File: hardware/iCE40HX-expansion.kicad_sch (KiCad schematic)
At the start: 3 parts, among them J1 EXT3, J2 EXT1, J4 VGA_Conn

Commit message: porgress with schematic
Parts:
- removed J4: VGA_Conn, symbol Connector:DE15_Plug_HighDensity_MountingHoles
- added C1, C10, C12, C14, C4, C5, C8: 0.1uf, Capacitor_SMD:C_0603_1608Metric, symbol Device:C_Small
- added C11, C13, C15, C6, C9: 10nf, Capacitor_SMD:C_0603_1608Metric, symbol Device:C_Small
- added C2, C3: 47pf, Capacitor_SMD:C_0603_1608Metric, symbol Device:C_Small
- added C7: 82nf, Capacitor_SMD:C_0603_1608Metric, symbol Device:C_Small
- added J3, J5: AudioJack3_Ground, Connector_Audio:Jack_3.5mm_KoreanHropartsElec_PJ-320D-4A_Horizontal, symbol Connector_Audio:AudioJack3_Ground
- added J4: Conn_01x34, C2797218:FPC-SMD_KH-FG0.5-H2.0-34PIN, symbol Connector_Generic:Conn_01x34
- added J6: Conn_01x04, Connector_PinHeader_2.54mm:PinHeader_1x04_P2.54mm_Vertical, symbol Connector_Generic:Conn_01x04
- added J7: Conn_01x06, Connector_PinHeader_2.54mm:PinHeader_1x06_P2.54mm_Vertical, symbol Connector_Generic:Conn_01x06
- added R1, R4: 39, Resistor_SMD:R_0603_1608Metric, symbol Device:R_Small
- added R10, R11, R12, R13, R14, R15, R16, R17, R18, R19, R20, R21, R22, R23, R24, R25, R26, R27, R28, R29, R30, R6, R7, R8, R9: 470, Resistor_SMD:R_0603_1608Metric, symbol Device:R_Small
- added R2, R3: 36, Resistor_SMD:R_0603_1608Metric, symbol Device:R_Small
- added R5: 1.69k, Resistor_SMD:R_0603_1608Metric, symbol Device:R_Small
- added U1: ADV7180BCP32Z-RL, C459884:LFCSP-32_L5.0-W5.0-P0.50-BL-EP3.6, symbol C459884:ADV7180BCP32Z-RL
- added U2: AMS1117-1.8, Package_TO_SOT_SMD:SOT-223-3_TabPin2, symbol Regulator_Linear:AMS1117-1.8
- added Y1: 28.63636MHz, Crystal:Crystal_SMD_Abracon_ABM8AIG-4Pin_3.2x2.5mm, symbol Device:Crystal_GND24_Small
- J1, J2: footprint (none) -> Connector_PinSocket_1.27mm:PinSocket_2x20_P1.27mm_Vertical_SMD
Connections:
- net +3V3: now also C8.1, C9.1, U1.3 (DVDDIO)
- net +5V: now also J4.31 (Pin_31), J4.32 (Pin_32), J4.33 (Pin_33), J4.34 (Pin_34)
- net BLUE: now also J7.1 (Pin_1)
- net GND: now also C10.2, C11.2, C12.2, C13.2, C14.2, C15.2, C2.2, C3.2, C8.2, C9.2, J3.G, J4.1 (Pin_1), J4.30 (Pin_30), J5.G, J6.4 (Pin_4), J7.6 (Pin_6), R1.2, R30.2, R4.2, U1.2 (DGND), U1.26 (ALSB), U1.29 (AIN2), U1.33 (EP), Y1.2, Y1.4
- net GREEN: now also J7.2 (Pin_2)
- net Hsync: now also J7.5 (Pin_5)
- net PIO0_00: now also R6.2
- net PIO0_01: now also R7.2
- net PIO0_02: now also R8.2
- net PIO0_03: now also R9.2
- net PIO0_04: now also R10.2
- net PIO0_05: now also R11.2
- net PIO0_06: now also R12.2
- net PIO0_07: now also R13.2
- net RED: now also J7.3 (Pin_3)
- net Vsync: now also J7.4 (Pin_4)
- new net: C3.1, U1.13 (XTAL), Y1.3
- new net: R29.2, R30.1
- new net: R20.1, R27.1, R28.2
- new net: R12.1, R20.2
- new net: R17.1, R24.1, R25.2
- new net: R16.1, R23.1, R24.2
- new net: J5.T, R3.1
- new net: C5.2, R3.2, R4.1
- new net: R14.2, R6.1
- new net: R15.2, R7.1
- new net: R11.1, R19.2
- new net: R16.2, R8.1
- new net: R19.1, R26.1, R27.2
- new net: C6.2, R5.1, U1.17 (ELPF)
- new net: C4.2, R1.1, R2.2
- new net: R13.1, R21.2
- new net: R17.2, R9.1
- new net: R21.1, R28.1
- new net: C7.2, R5.2
- new net: R14.1, R22.2, R29.1
- new net: R18.1, R25.1, R26.2
- new net: R10.1, R18.2
- new net: R15.1, R22.1, R23.2
- new net: C2.1, U1.12 (XTAL1), Y1.1
- new net: J3.T, R2.1
- new net: C1.2, U1.20 (VREFP)
- new net: C1.1, U1.21 (VREFN)
- new net +1V8: C10.1, C11.1, C12.1, C13.1, C14.1, C15.1, C6.1, C7.1, U1.14 (DVDD), U1.18 (PVDD), U1.22 (AVDD), U1.30 (AIN3)
- new net AIN1: C4.1, U1.23 (AIN1)
- new net AIN2: C5.1, U1.29 (AIN2)
- new net HS: U1.1 (HS)
- new net INTRQ: U1.32 (~{INTRQ})
- new net LLC: U1.11 (LLC)
- new net RGB_B0: J4.6 (Pin_6)
- new net RGB_B1: J4.7 (Pin_7)
- new net RGB_B2: J4.8 (Pin_8)
- new net RGB_B3: J4.9 (Pin_9)
- new net RGB_B4: J4.10 (Pin_10)
- new net RGB_B5: J4.11 (Pin_11)
- new net RGB_B6: J4.12 (Pin_12)
- new net RGB_B7: J4.13 (Pin_13)
- new net RGB_CLK: J4.2 (Pin_2)
- new net RGB_EN: J4.4 (Pin_4)
- new net RGB_G0: J4.14 (Pin_14)
- new net RGB_G1: J4.15 (Pin_15)
- new net RGB_G2: J4.16 (Pin_16)
- new net RGB_G3: J4.17 (Pin_17)
- new net RGB_G4: J4.18 (Pin_18)
- new net RGB_G5: J4.19 (Pin_19)
- new net RGB_G6: J4.20 (Pin_20)
- new net RGB_G7: J4.21 (Pin_21)
- new net RGB_HSYNC: J4.3 (Pin_3)
- new net RGB_R0: J4.22 (Pin_22)
- new net RGB_R1: J4.23 (Pin_23)
- new net RGB_R2: J4.24 (Pin_24)
- new net RGB_R3: J4.25 (Pin_25)
- new net RGB_R4: J4.26 (Pin_26)
- new net RGB_R5: J4.27 (Pin_27)
- new net RGB_R6: J4.28 (Pin_28)
- new net RGB_R7: J4.29 (Pin_29)
- new net RGB_VSYNC: J4.5 (Pin_5)
- new net RST: J6.3 (Pin_3), U1.25 (~{RESET})
- new net SCLK: J6.1 (Pin_1), U1.28 (SCLK)
- new net SDATA: J6.2 (Pin_2), U1.27 (SDATA)
- new net SFL: U1.4 (SFL)
- new net VS: U1.31 (VS/FIELD)
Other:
- note added: "ADDR = 40h"
- note added: "DECODER"
- note added: "EXTERNAL"
- note added: "RGB FPC"
- note removed: "VGA"

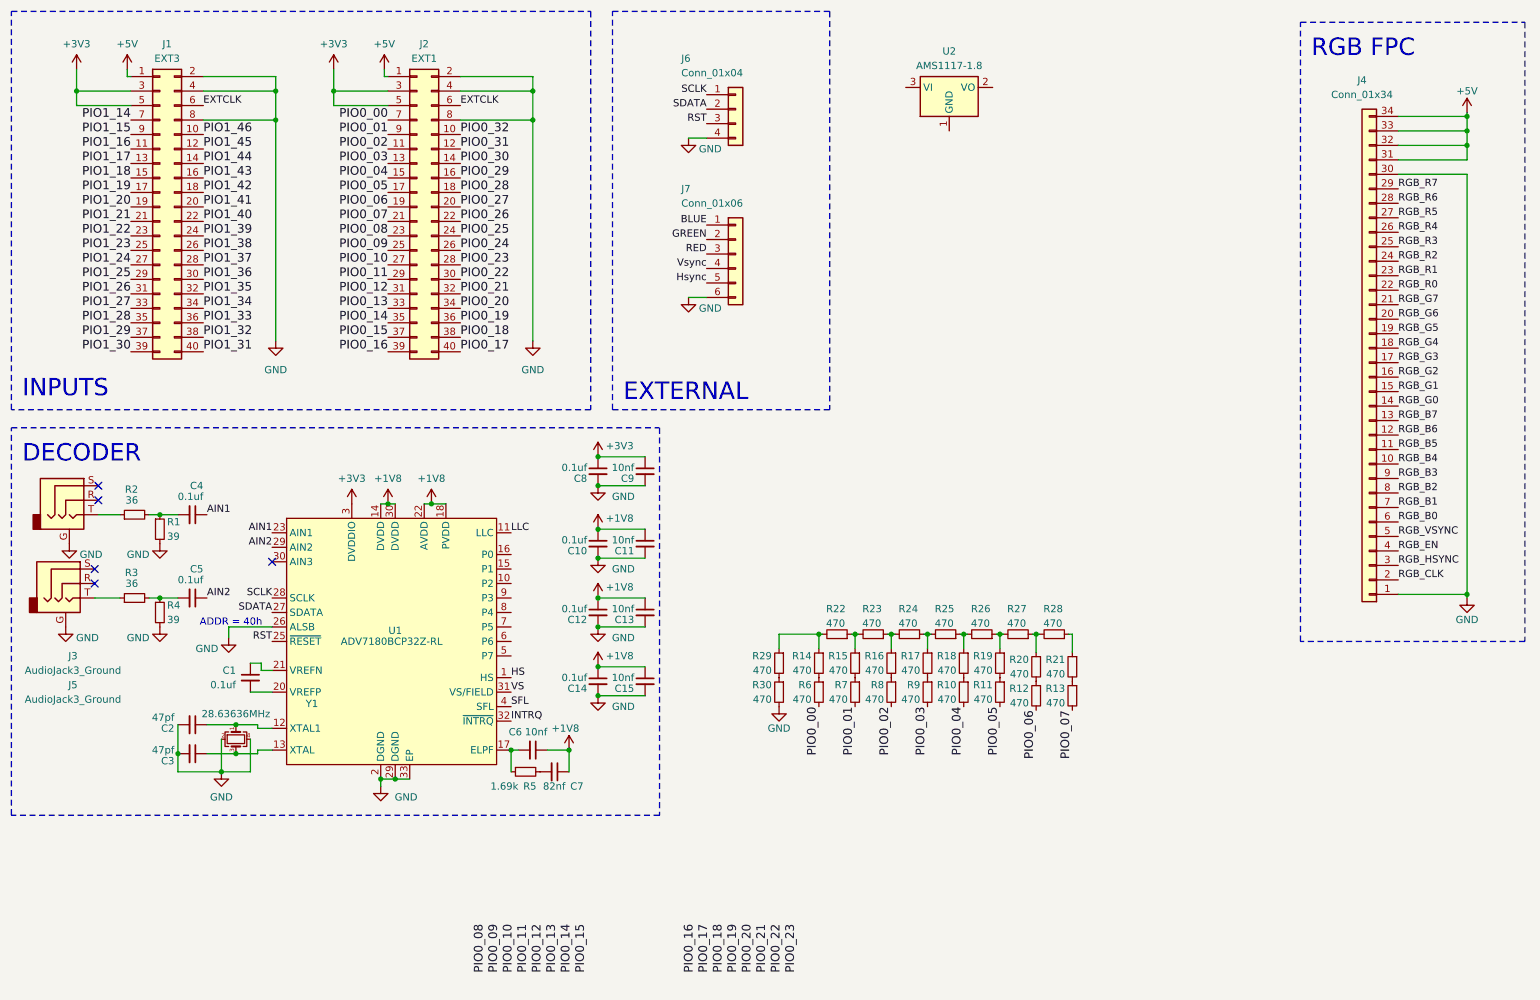
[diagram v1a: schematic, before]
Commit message: moved R2R dacs into hierarchical sheets
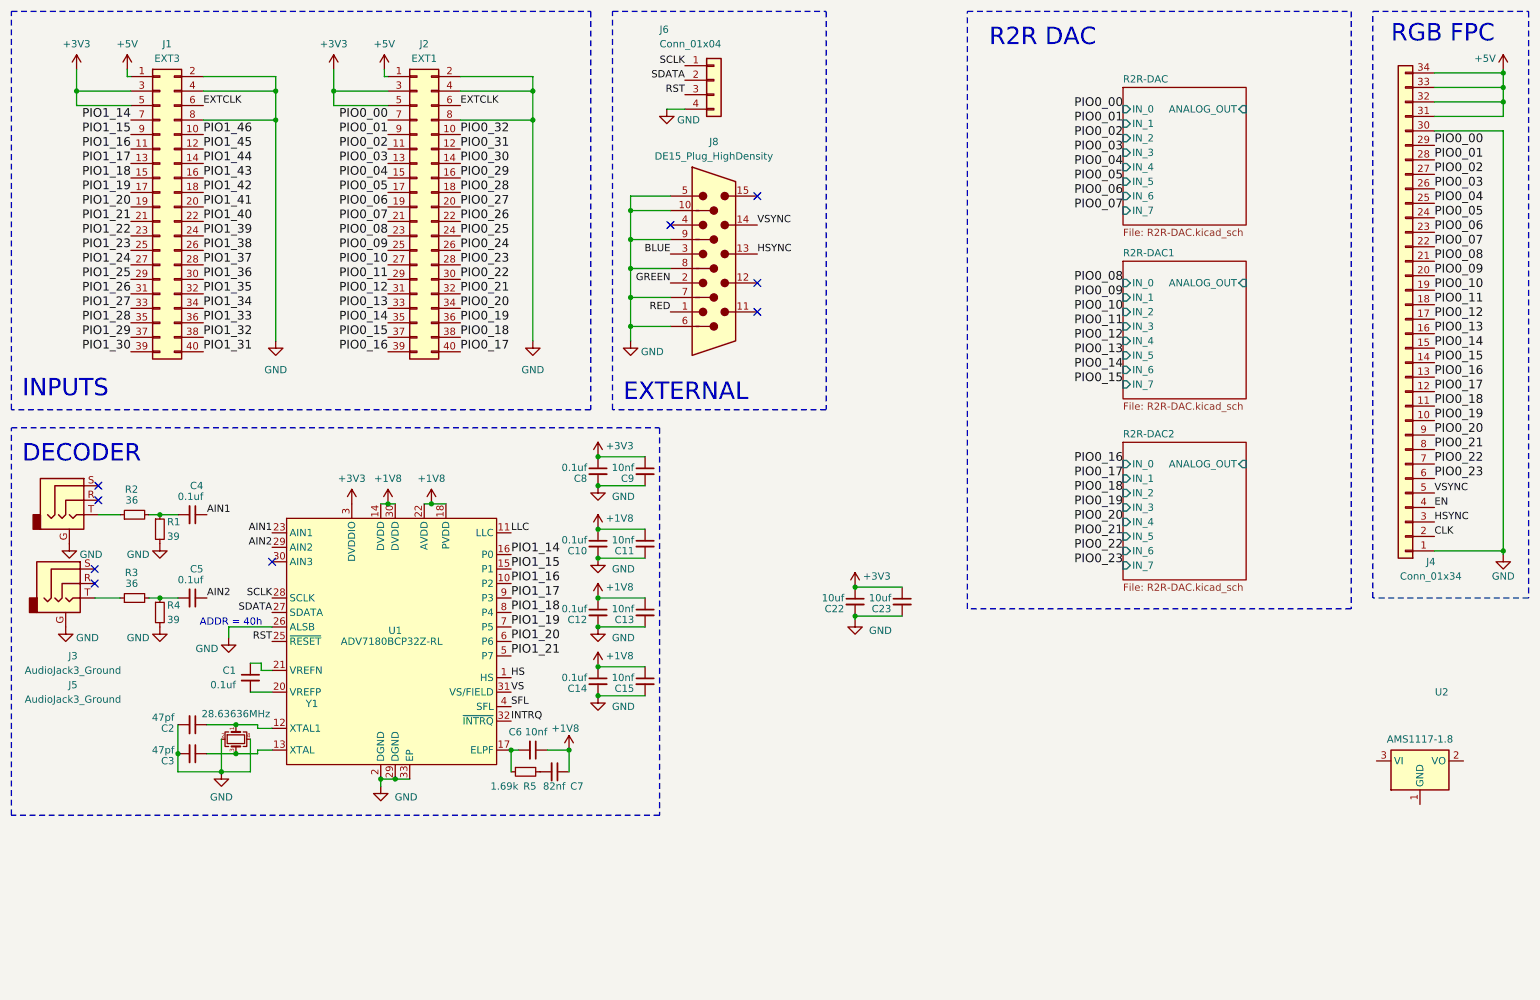
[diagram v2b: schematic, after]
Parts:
- removed J7: Conn_01x06, Connector_PinHeader_2.54mm:PinHeader_1x06_P2.54mm_Vertical, symbol Connector_Generic:Conn_01x06
- removed R10, R11, R12, R13, R14, R15, R16, R17, R18, R19, R20, R21, R22, R23, R24, R25, R26, R27, R28, R29, R30, R6, R7, R8, R9: 470, Resistor_SMD:R_0603_1608Metric, symbol Device:R_Small
- added C22, C23: 10uf, Capacitor_SMD:C_0603_1608Metric, symbol Device:C_Small
- added J8: DE15_Plug_HighDensity, C711364:DSUB-TH_HYC06-HDR15B-060, symbol Connector:DE15_Plug_HighDensity
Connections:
- net RGB_B0 is gone; now on net PIO0_23: J4.6 (Pin_6)
- net RGB_B1 is gone; now on net PIO0_22: J4.7 (Pin_7)
- net RGB_B2 is gone; now on net PIO0_21: J4.8 (Pin_8)
- net RGB_B3 is gone; now on net PIO0_20: J4.9 (Pin_9)
- net RGB_B4 is gone; now on net PIO0_19: J4.10 (Pin_10)
- net RGB_B5 is gone; now on net PIO0_18: J4.11 (Pin_11)
- net RGB_B6 is gone; now on net PIO0_17: J4.12 (Pin_12)
- net RGB_B7 is gone; now on net PIO0_16: J4.13 (Pin_13)
- net RGB_G0 is gone; now on net PIO0_15: J4.14 (Pin_14)
- net RGB_G1 is gone; now on net PIO0_14: J4.15 (Pin_15)
- net RGB_G2 is gone; now on net PIO0_13: J4.16 (Pin_16)
- net RGB_G3 is gone; now on net PIO0_12: J4.17 (Pin_17)
- net RGB_G4 is gone; now on net PIO0_11: J4.18 (Pin_18)
- net RGB_G5 is gone; now on net PIO0_10: J4.19 (Pin_19)
- net RGB_G6 is gone; now on net PIO0_09: J4.20 (Pin_20)
- net RGB_G7 is gone; now on net PIO0_08: J4.21 (Pin_21)
- net RGB_R0 is gone; now on net PIO0_07: J4.22 (Pin_22)
- net RGB_R1 is gone; now on net PIO0_06: J4.23 (Pin_23)
- net RGB_R2 is gone; now on net PIO0_05: J4.24 (Pin_24)
- net RGB_R3 is gone; now on net PIO0_04: J4.25 (Pin_25)
- net RGB_R4 is gone; now on net PIO0_03: J4.26 (Pin_26)
- net RGB_R5 is gone; now on net PIO0_02: J4.27 (Pin_27)
- net RGB_R6 is gone; now on net PIO0_01: J4.28 (Pin_28)
- net RGB_R7 is gone; now on net PIO0_00: J4.29 (Pin_29)
- net +3V3: now also C22.1, C23.1
- net BLUE: now also J8.3
- net GND: now also C22.2, C23.2, J8.10, J8.5, J8.6, J8.7, J8.8, J8.9
- net GREEN: now also J8.2
- net PIO1_14: now also U1.16 (P0)
- net PIO1_15: now also U1.15 (P1)
- net PIO1_16: now also U1.10 (P2)
- net PIO1_17: now also U1.9 (P3)
- net PIO1_18: now also U1.8 (P4)
- net PIO1_19: now also U1.7 (P5)
- net PIO1_20: now also U1.6 (P6)
- net PIO1_21: now also U1.5 (P7)
- net RED: now also J8.1
- net RGB_CLK renamed CLK
- net RGB_EN renamed EN
- net RGB_HSYNC renamed HSYNC
- net HSYNC: now also J8.13
- net RGB_VSYNC renamed VSYNC
- net VSYNC: now also J8.14
- no-connect marks 5 -> 9
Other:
- added sheet R2R-DAC (R2R-DAC.kicad_sch)
- added sheet R2R-DAC1 (R2R-DAC.kicad_sch)
- added sheet R2R-DAC2 (R2R-DAC.kicad_sch)
- note added: "R2R DAC"
- moved on the sheet: J4, J6, U2
